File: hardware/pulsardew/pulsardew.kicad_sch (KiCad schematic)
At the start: 12 parts, among them J1 USB-C, J2 DC-005 2.0mm, J3 Phoenix 2-pos, U1 STM32G0B1KBU6

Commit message: hardware: wire and verify the PulsarDew schematic hierarchy
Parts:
- removed C1, C2: 100n, Capacitor_SMD:C_0402_1005Metric, symbol Device:C
- removed J1: USB-C, Connector_USB:USB_C_Receptacle_GCT_USB4105-xx-A_16P_TopMnt_Horizontal, symbol Connector:USB_C_Receptacle_USB2.0_16P
- removed R10, R11: 5.1k, Resistor_SMD:R_0402_1005Metric, symbol Device:R
- removed R20, R21: 4.7k, Capacitor_SMD:C_0402_1005Metric, symbol Device:R
- removed U1: STM32G0B1KBU6, pulsarfab:UFQFPN-32, symbol pulsarfab:STM32G0B1KBU6
- J3: footprint Connector_Phoenix_MKDS:PhoenixContact_MKDS_3,2-5,08_1x02_P5.08mm_Horizontal -> TerminalBlock_Phoenix:TerminalBlock_Phoenix_MKDS-1,5-2-5.08_1x02_P5.08mm_Horizontal; LCSC C480537 -> (none); MPN 1803277 -> (none)
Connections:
- net VIN_PROT: now also C10.1, D10.1 (K)
- new net: D10.2 (A), J2.1, J3.1 (Pin_1)
- new net GND: C10.2, J2.2, J3.2 (Pin_2)
- no-connect marks 2 -> 1
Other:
- added sheet Controller (controller.kicad_sch)
- sheet Current Sense ports: added VDD; removed +3V3
- sheet Heater Ch0 ports: added VDD; removed +3V3, HEATER
- sheet Heater Ch1 ports: added VDD; removed +3V3, HEATER
- sheet Heater Ch2 ports: added VDD; removed +3V3, HEATER
- sheet Heater Ch3 ports: added VDD; removed +3V3, HEATER
- sheet LDO 3.3V ports: added VDD; removed +3V3
- sheet SHT40 ports: added VDD; removed +3V3
- note added: "12-20 V DC input. Logic supply and heater current paths are separate after reverse-polarity protection."
- note added: "CHANNELS 0: J101 / Q102 / PA0 1: J201 / Q202 / PA1 2: J301 / Q302 / PA2 3: J401 / Q402 / PA3"
- note added: "PULSARDEW | USB dew-heater controller"
- note added: "Supply: J2 or J3 (one source). D10 protects polarity. VIN_HEAT feeds all four heater connectors through R30. One INA226 measures total heater current, excluding the logic LDO. Current rating is limited by connectors, diode, shunt and PCB thermals."
- note removed: "Power Input: 12-20V DC via barrel jack or Phoenix terminal"
- note removed: "PulsarDew — USB Dew Heater Controller"
- note removed: "SS54 reverse polarity protection + 470µF bulk cap"
- note removed: "STM32G0B1KBU6 + USB-C + 4× heater channels + INA226 current sense + SHT40"
- company: (none) -> PulsarFab
- title: PulsarDew — USB Dew Heater Controller -> PulsarDew - System wiring

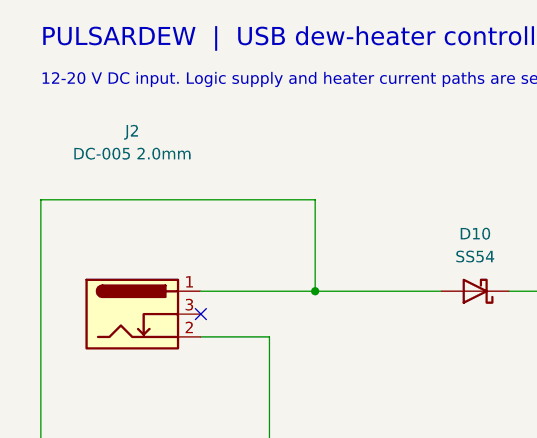
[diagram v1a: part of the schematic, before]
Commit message: Match PulsarDew connector sourcing to reviewed footprints
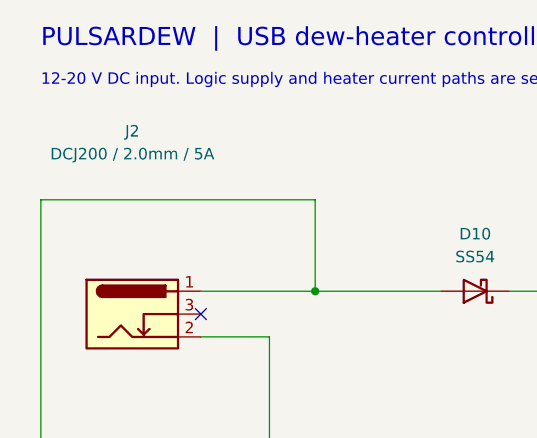
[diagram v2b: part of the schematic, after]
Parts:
- J2: value DC-005 2.0mm -> DCJ200 / 2.0mm / 5A; LCSC C2880546 -> C5280493; MPN DC-005K-5A-2.0 -> DCJ200-10-A-K1-K; Manufacturer (none) -> GCT
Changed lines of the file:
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@@
       (font
         (size 1.27 1.27))))
-  (property "Value" "DC-005 2.0mm"
+  (property "Value" "DCJ200 / 2.0mm / 5A"
     (at 30.48 30.48 0.0)
     (effects
@@
         (size 1.27 1.27))
       (hide yes)))
-  (property "Datasheet" ""
+  (property "Datasheet" "https://gct.co/files/drawings/dcj200.pdf"
     (at 30.48 48.26 0.0)
     (effects
@@
         (size 1.27 1.27))
       (hide yes)))
-  (property "LCSC" "C2880546"
+  (property "LCSC" "C5280493"
     (at 30.48 48.26 0.0)
     (effects
@@
         (size 1.27 1.27))
       (hide yes)))
-  (property "MPN" "DC-005K-5A-2.0"
+  (property "MPN" "DCJ200-10-A-K1-K"
     (at 30.48 48.26 0.0)
     (effects
@@
       (path "/4235aaa6-671a-4985-9062-abb1f1decfe0"
         (reference "J2")
-        (unit 1)))))
+        (unit 1))))(property "Manufacturer" "GCT"
+  (at 30.48 48.26 0.0)
+  (effects
+    (font
+      (size 1.27 1.27))
+    (hide yes)))
+	)
 (symbol
   (lib_id "Connector_Generic:Conn_01x02")

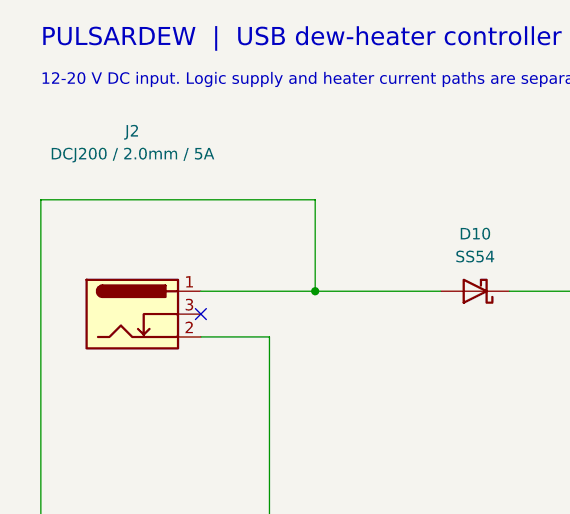
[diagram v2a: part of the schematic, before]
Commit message: Use owned XKB barrel sockets and evaluate LMR51610 commonality
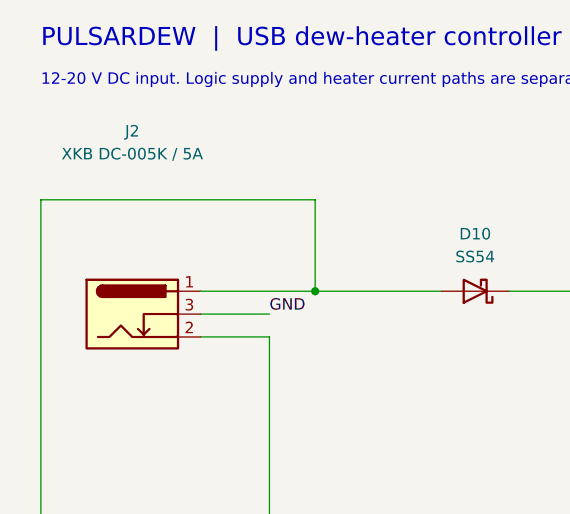
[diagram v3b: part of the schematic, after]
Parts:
- J2: value DCJ200 / 2.0mm / 5A -> XKB DC-005K / 5A; footprint Connector_BarrelJack:BarrelJack_GCT_DCJ200-10-A_Horizontal -> pulsarfab:BarrelJack_XKB_DC-005K-5A_Edge; LCSC C5280493 -> C2880546; MPN DCJ200-10-A-K1-K -> DC-005K-5A-2.0; Manufacturer GCT -> XKB Connection
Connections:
- net GND: now also J2.3
- no-connect marks 1 -> 0
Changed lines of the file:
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@@
       (font
         (size 1.27 1.27))))
-  (property "Value" "DCJ200 / 2.0mm / 5A"
+  (property "Value" "XKB DC-005K / 5A"
     (at 30.48 30.48 0.0)
     (effects
       (font
         (size 1.27 1.27))))
-  (property "Footprint" "Connector_BarrelJack:BarrelJack_GCT_DCJ200-10-A_Horizontal"
-    (at 30.48 48.26 0.0)
-    (effects
-      (font
-        (size 1.27 1.27))
-      (hide yes)))
-  (property "Datasheet" "https://gct.co/files/drawings/dcj200.pdf"
-    (at 30.48 48.26 0.0)
-    (effects
-      (font
-        (size 1.27 1.27))
-      (hide yes)))
-  (property "Description" ""
-    (at 30.48 48.26 0.0)
-    (effects
-      (font
-        (size 1.27 1.27))
-      (hide yes)))
-  (property "LCSC" "C5280493"
-    (at 30.48 48.26 0.0)
-    (effects
-      (font
-        (size 1.27 1.27))
-      (hide yes)))
-  (property "MPN" "DCJ200-10-A-K1-K"
+  (property "Footprint" "pulsarfab:BarrelJack_XKB_DC-005K-5A_Edge"
+    (at 30.48 48.26 0.0)
+    (effects
+      (font
+        (size 1.27 1.27))
+      (hide yes)))
+  (property "Datasheet" "https://datasheet.lcsc.com/datasheet/pdf/42a925a8542473f46554cf6f67b6cc91.pdf?productCode=C2880546"
+    (at 30.48 48.26 0.0)
+    (effects
+      (font
+        (size 1.27 1.27))
+      (hide yes)))
+  (property "Description" ""
+    (at 30.48 48.26 0.0)
+    (effects
+      (font
+        (size 1.27 1.27))
+      (hide yes)))
+  (property "LCSC" "C2880546"
+    (at 30.48 48.26 0.0)
+    (effects
+      (font
+        (size 1.27 1.27))
+      (hide yes)))
+  (property "MPN" "DC-005K-5A-2.0"
     (at 30.48 48.26 0.0)
     (effects
@@
       (path "/4235aaa6-671a-4985-9062-abb1f1decfe0"
         (reference "J2")
-        (unit 1))))(property "Manufacturer" "GCT"
+        (unit 1))))(property "Manufacturer" "XKB Connection"
   (at 30.48 48.26 0.0)
   (effects
@@
         (reference "C10")
         (unit 1)))))
-(no_connect (at 38.1000 48.2600))
+(wire (pts (xy 38.1 48.26) (xy 45.72 48.26)) (stroke (width 0) (type default)))
+(label "GND" (at 45.72 48.26 0) (effects (font (size 1.27 1.27)) (justify left bottom)))
 (label "GND"  (at 45.7200 101.6000 0) (effects (font (size 1.27 1.27)) (justify left bottom)))
 (symbol
